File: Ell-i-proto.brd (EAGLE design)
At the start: 101.6 x 53.3 mm, 133 parts, among them J1 PROG, J10 PJ-102AX, J11 48V, J2 PWMH, J3 PWR, J4 PWML, J5 ANAL, J6 SPI, J7 COMM, J8 ANAH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

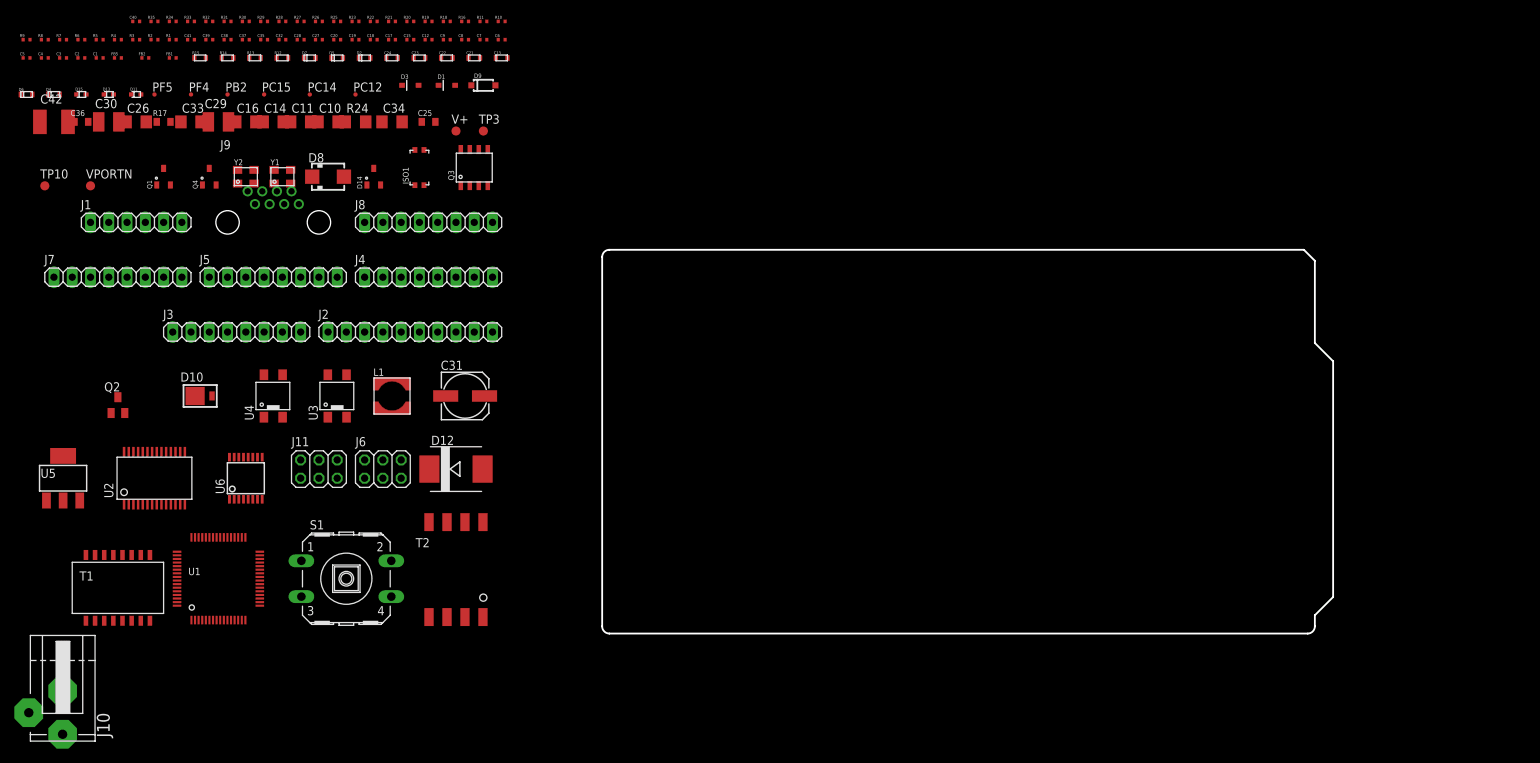
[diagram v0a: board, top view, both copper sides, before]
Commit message: Due connectors in Due positions, some drafting for other compos
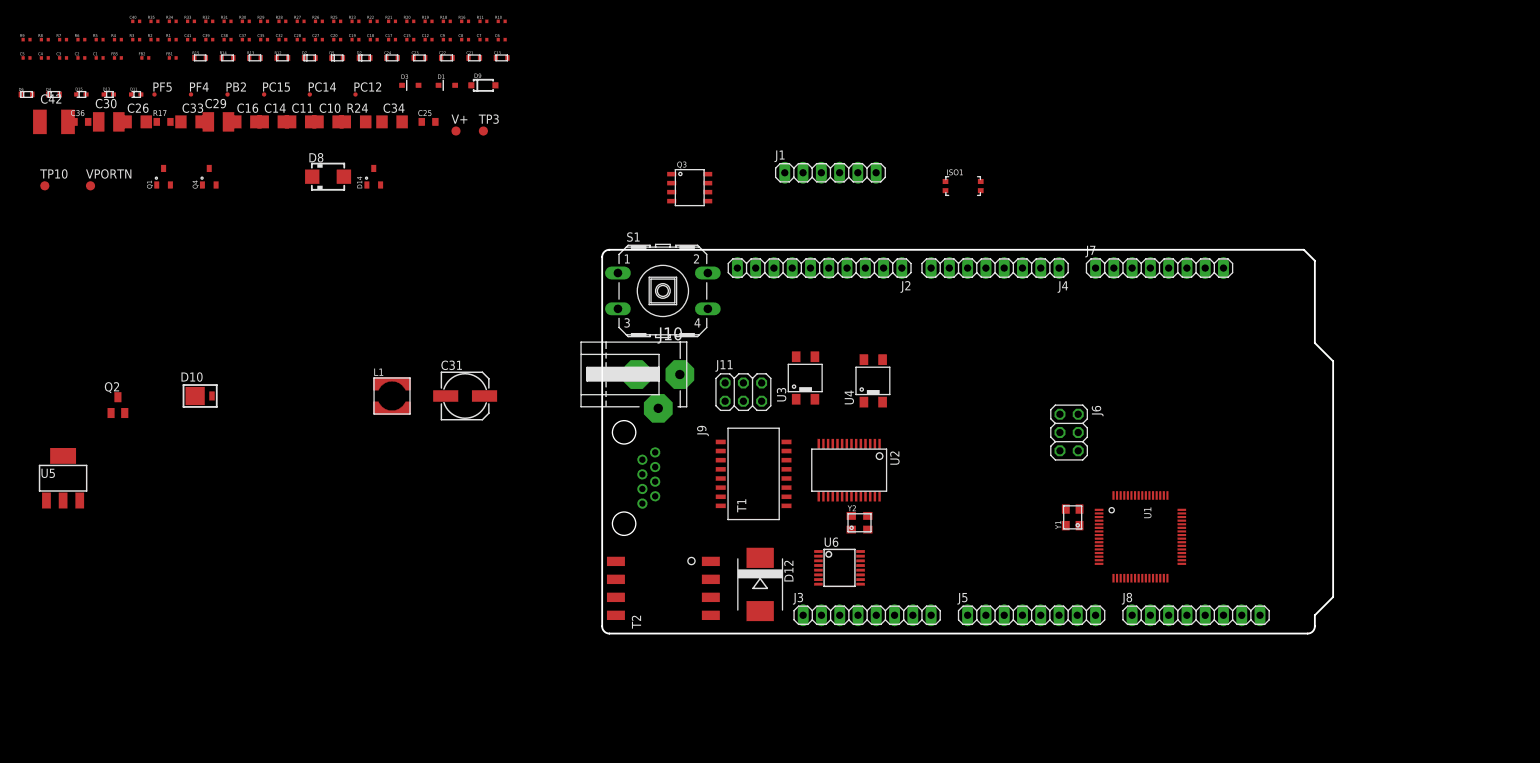
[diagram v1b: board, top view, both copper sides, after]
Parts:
- moved J7 144.8 mm to (77.5, 50.8)
- moved U1 128.3 mm to (74.8, 13.4), turned to 270 degrees
- moved J8 119.8 mm to (82.5, 2.54)
- moved Y1 119.6 mm to (65.4, 16.1), turned to 90 degrees
- moved J5 115.4 mm to (59.7, 2.54)
- moved Y2 97.9 mm to (35.8, 15.4)
- moved J1 96.7 mm to (31.7, 64.0)
- moved U2 96.6 mm to (34.3, 22.7), turned to 180 degrees
- moved J3 96.1 mm to (36.8, 2.54)
- moved J6 95.5 mm to (64.9, 27.9), turned to 270 degrees
- moved J10 90.7 mm to (4.50, 36.0), turned to 90 degrees
- moved T1 89.8 mm to (21.1, 22.2), turned to 90 degrees
- moved U6 83.5 mm to (33.0, 9.13), turned to 270 degrees
- moved U4 83.4 mm to (37.7, 35.1)
- moved J4 78.8 mm to (54.6, 50.8), turned to 180 degrees
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
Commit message: mounting holes, S1 & FTDI conn updated, drafting the placements & GND area, etc
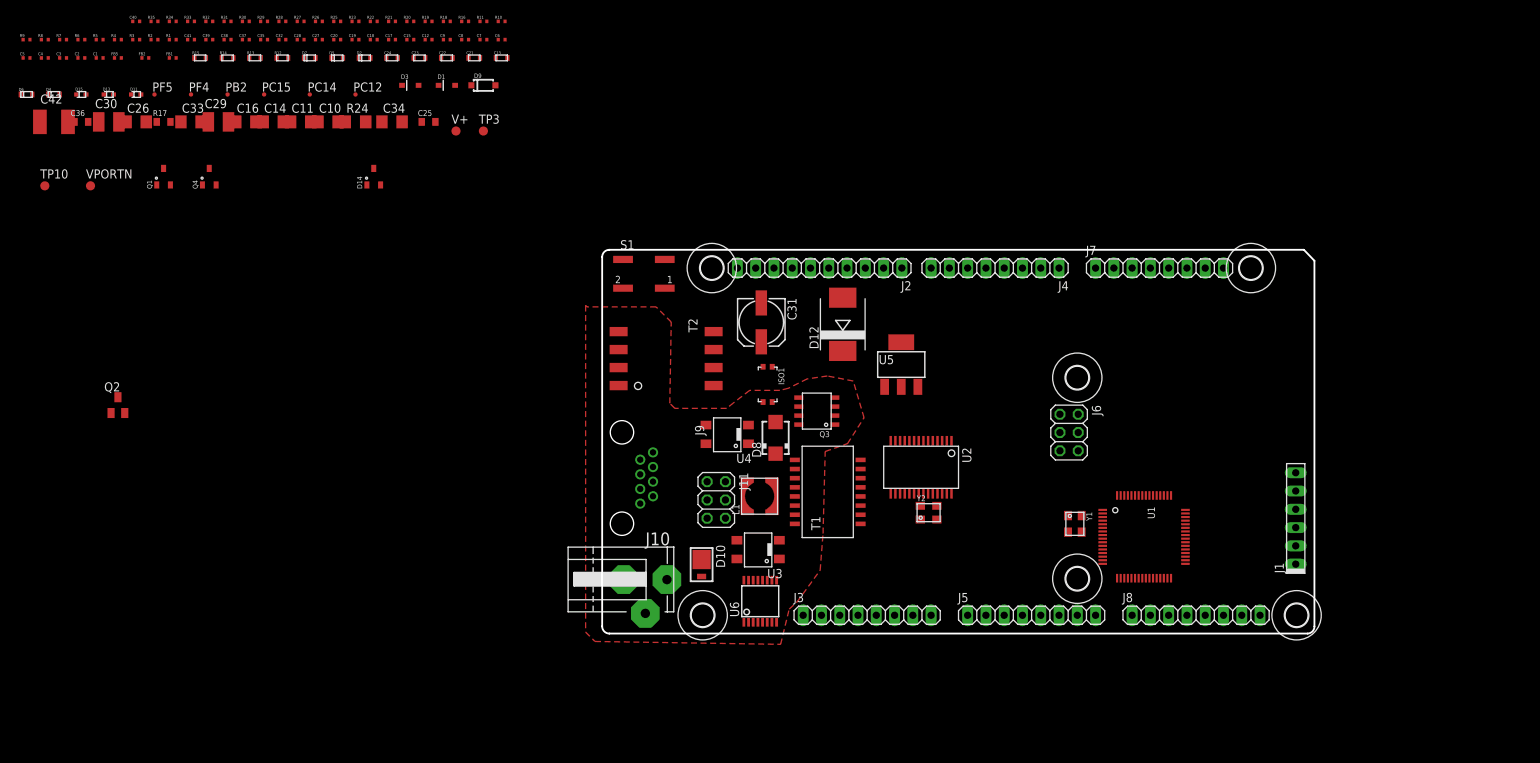
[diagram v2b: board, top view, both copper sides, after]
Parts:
- added H1, H2, H3, H4, H5, H6: MOUNT-HOLE3.2, holes:3,2
- J1: value PROG -> FTDI-SER-6; device ell-i:1X06 -> ell-i:FTDI-SER-6
- Q2: value MMTBA42 -> MMBTA42
- S1: value RACON12 -> B3SL-10X2P; device switch-misc:RACON12 -> ell-i:B3SL-10X2P
- moved U5 117.6 mm to (41.6, 37.4)
- moved J1 80.6 mm to (96.4, 16.0), turned to 90 degrees
- moved D10 73.5 mm to (13.8, 9.58), turned to 270 degrees
- moved D8 72.0 mm to (24.1, 27.2), turned to 90 degrees
- moved L1 53.0 mm to (21.9, 19.1), turned to 90 degrees
- moved C31 42.4 mm to (22.1, 43.2), turned to 270 degrees
- moved ISO1 38.7 mm to (23.0, 34.6), turned to 180 degrees
- moved D12 37.9 mm to (33.4, 43.0), turned to 90 degrees
- moved Q3 35.7 mm to (29.8, 30.9), turned to 90 degrees
- moved T2 31.9 mm to (8.89, 38.2), turned to 270 degrees
- moved J10 28.6 mm to (2.70, 7.50)
- moved U3 24.7 mm to (21.7, 11.7), turned to 90 degrees
- moved U4 21.6 mm to (17.4, 27.7), turned to 90 degrees
- moved J11 15.5 mm to (15.9, 18.6), turned to 270 degrees
- moved U6 12.0 mm to (22.0, 4.49), turned to 0 degrees
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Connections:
- net GNDI: now also J1.GND, S1.1, S1.2; no longer J1.1, S1.3, S1.4
- net N$6: now also J1.-CTS; no longer J1.2
- net NDSR2: now also J1.-RTS; no longer J1.6
- net NRES: now also S1.3, S1.4; no longer S1.1, S1.2
- net RX2: now also J1.TXD; no longer J1.4
- net TX2: now also J1.RXD; no longer J1.5
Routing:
- added copper zone on layer 1, net GND
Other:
- board size 101.6 x 53.3 mm -> 99 x 53.3 mm

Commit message: drafting still, most components inside board edges, and T2 still on left edge
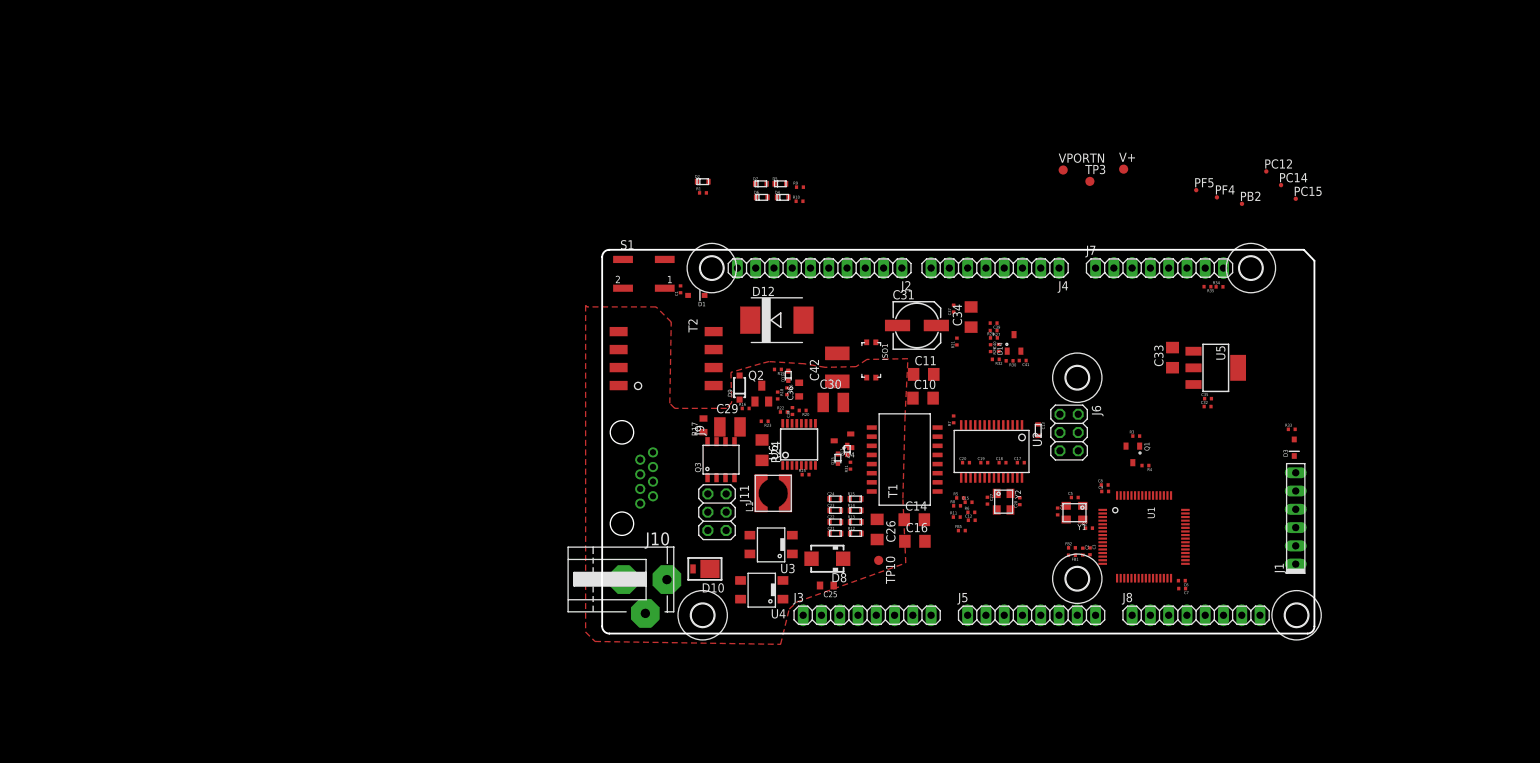
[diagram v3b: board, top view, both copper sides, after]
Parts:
- moved R33 163.2 mm to (95.8, 28.4)
- moved C3 158.4 mm to (67.8, 11.4), turned to 270 degrees
- moved C5 158.0 mm to (65.7, 18.9)
- moved C2 155.2 mm to (66.8, 11.4), turned to 270 degrees
- moved R4 154.6 mm to (75.5, 23.4), turned to 180 degrees
- moved C4 154.2 mm to (63.3, 17.0), turned to 270 degrees
- moved R35 150.9 mm to (84.1, 48.2), turned to 180 degrees
- moved R34 150.1 mm to (85.8, 48.2)
- moved R3 149.5 mm to (74.2, 27.4)
- moved R2 146.6 mm to (67.7, 14.7)
- moved FB2 145.7 mm to (65.3, 11.9)
- moved PF5 145.4 mm to (82.6, 61.6)
- moved PC15 144.1 mm to (96.4, 60.4)
- moved PF4 143.3 mm to (85.5, 60.6)
- moved FB1 142.8 mm to (65.3, 10.9), turned to 180 degrees
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
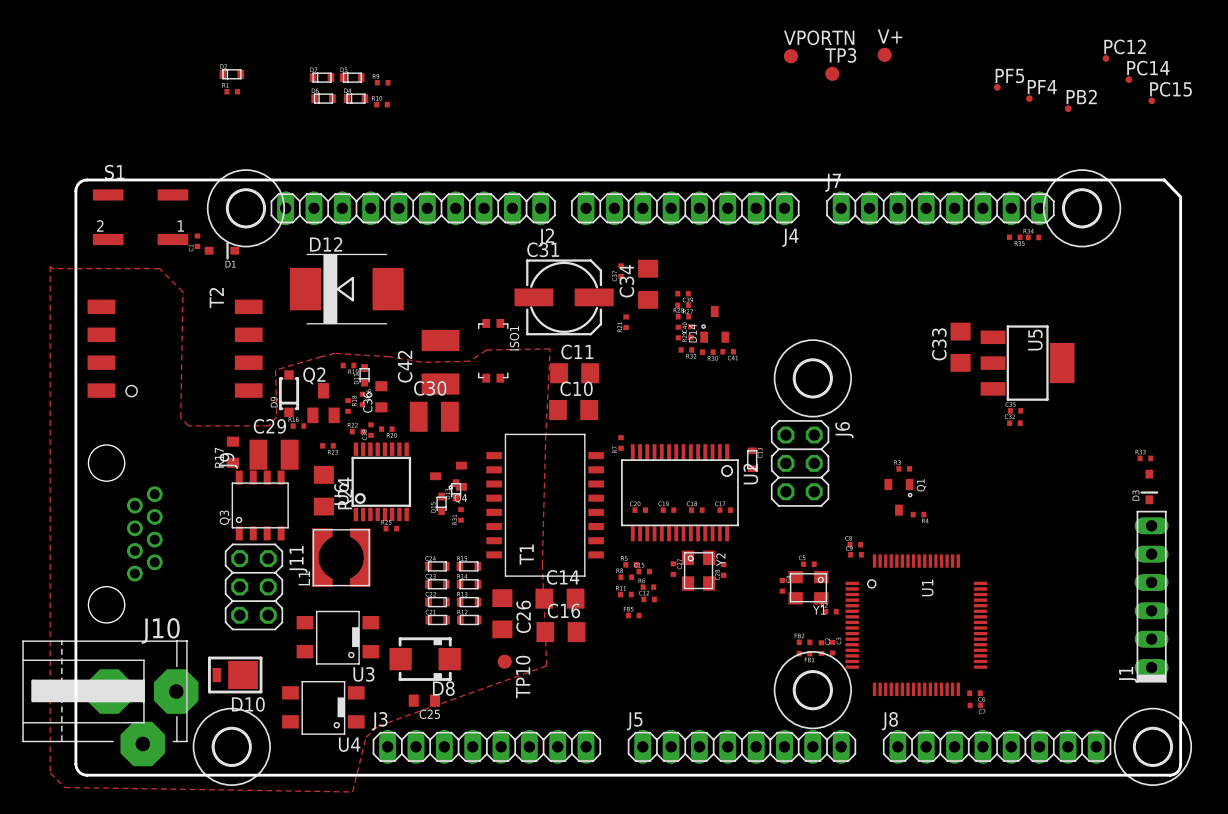
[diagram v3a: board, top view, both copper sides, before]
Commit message: rearrangement, T2 no more on the edge. Switch in 'location B', LEDs on the corner, etc
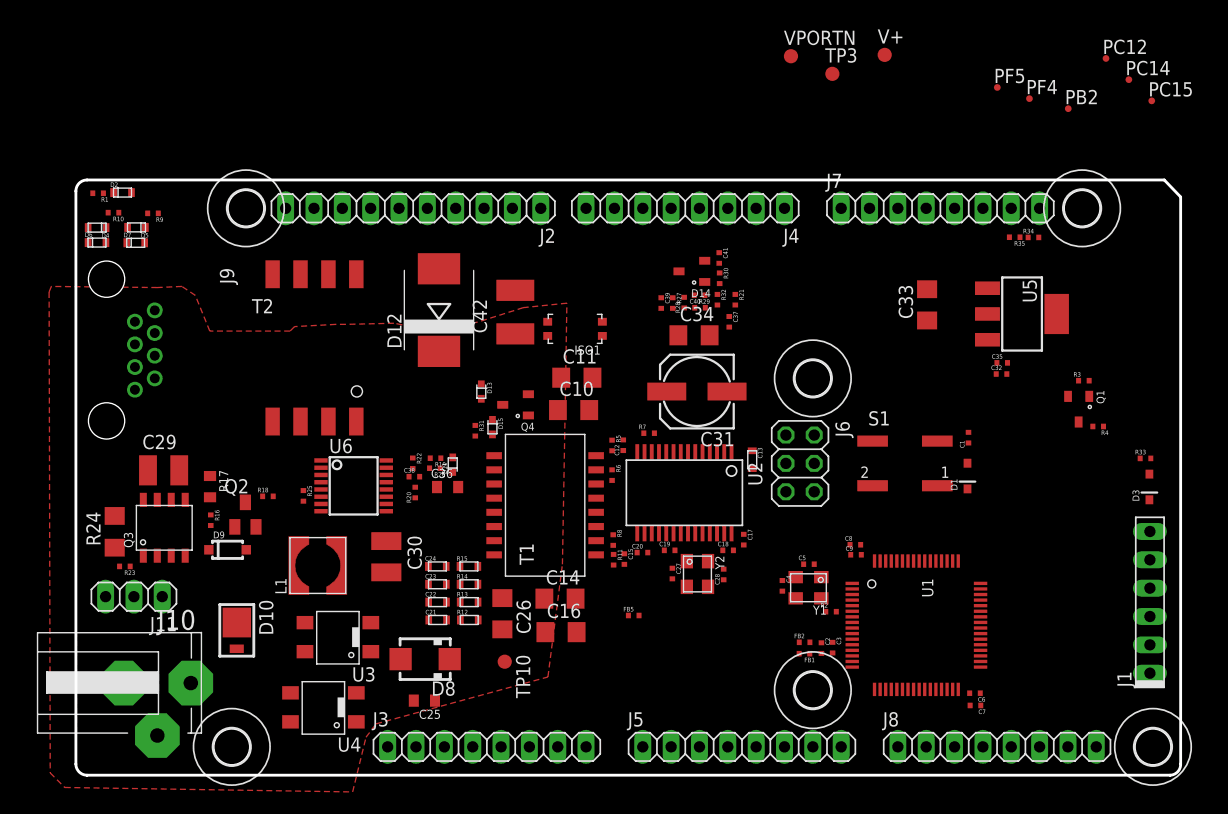
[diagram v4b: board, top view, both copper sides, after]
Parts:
- J11: value 48V -> (none); device ell-i:2X03 -> pinhead:1X03
- moved S1 72.0 mm to (74.3, 27.9)
- moved C1 71.3 mm to (80.0, 30.2)
- moved D1 69.8 mm to (79.9, 26.8), turned to 90 degrees
- moved R10 25.9 mm to (3.37, 50.4), turned to 180 degrees
- moved D4 25.9 mm to (1.90, 49.1), turned to 180 degrees
- moved D6 24.1 mm to (1.89, 47.7)
- moved R9 23.7 mm to (6.91, 50.4), turned to 180 degrees
- moved D5 23.5 mm to (5.43, 49.1), turned to 180 degrees
- moved D7 22.3 mm to (5.36, 47.7)
- moved R23 21.2 mm to (4.39, 18.7)
- moved R24 19.1 mm to (3.48, 21.8), turned to 90 degrees
- moved Q1 17.9 mm to (89.9, 32.8)
- moved R3 17.9 mm to (90.3, 35.4)
- moved R4 17.9 mm to (91.6, 31.2)
- moved J9 16.5 mm to (2.75, 38.1)
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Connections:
- net GND: now also J11.3; no longer J11.5, J11.6
- net NPWRGD: now also J11.2; no longer J11.3
- net V+: no longer J11.2

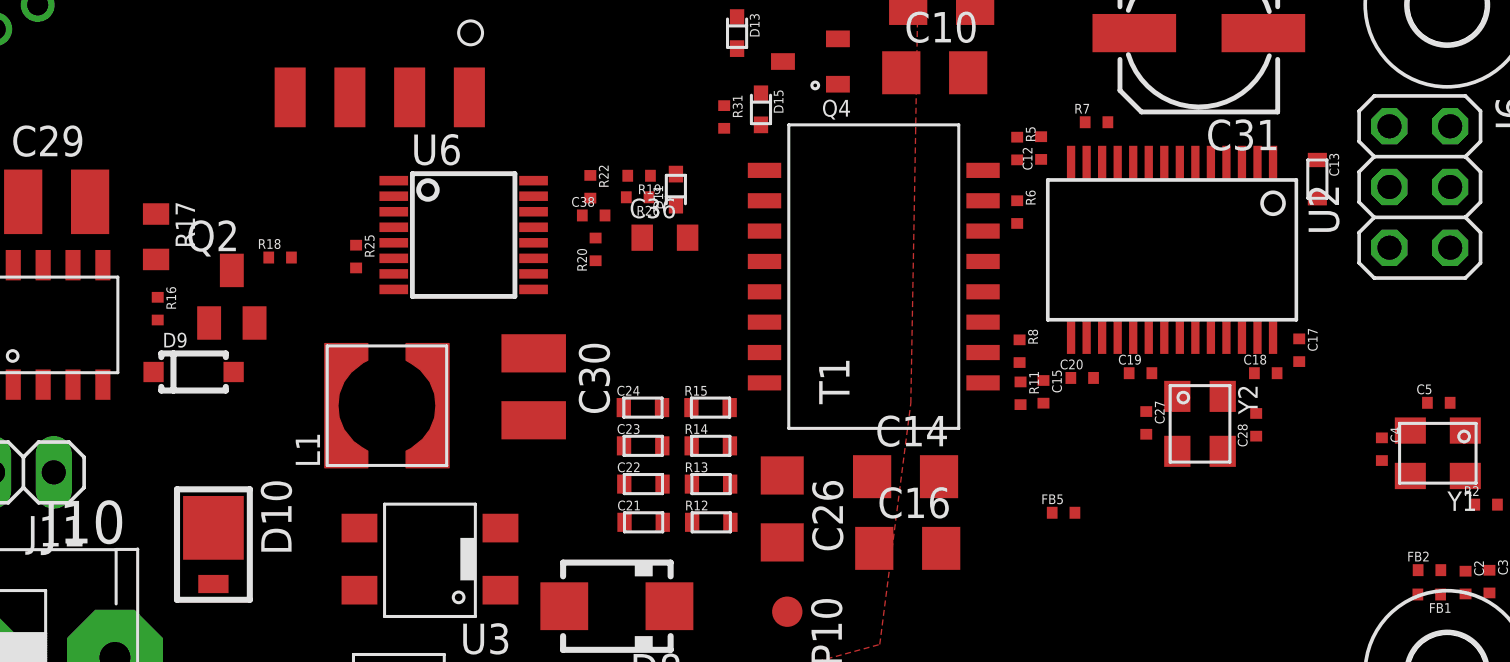
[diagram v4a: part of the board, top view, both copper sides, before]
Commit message: design rules added and applied to brd
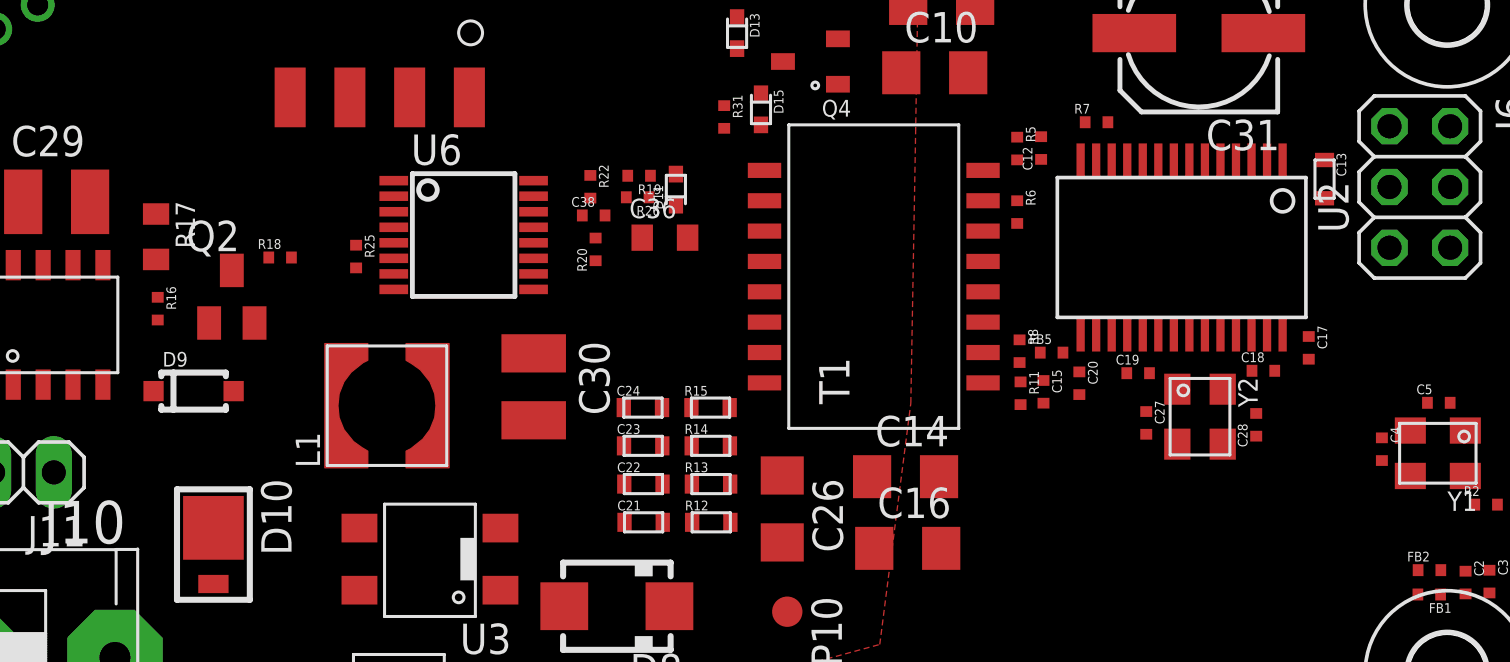
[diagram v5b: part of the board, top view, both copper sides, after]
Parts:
- moved FB5 6.72 mm to (49.5, 21.0)
- moved D9 0.80 mm to (13.6, 19.4)
- moved C17 0.41 mm to (60.2, 21.2)
- moved U2 0.41 mm to (54.9, 25.4)
- moved C13 0.30 mm to (60.9, 28.3)
- moved Y2 0.30 mm to (55.7, 18.3)
- moved C20 0.25 mm to (50.6, 19.7), turned to 270 degrees
- moved C18 0.14 mm to (58.4, 20.2)
- moved C19 0.10 mm to (53.1, 20.1)
